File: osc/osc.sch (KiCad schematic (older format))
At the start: 21 parts, among them P1 CONN_1, P2 CONN_1, P3 CONN_1, P4 CONN_1, P5 CONN_1, P6 CONN_5X2, Y1 ASOF3S3, Y2 AOCJYR, Y3 AST3TQ-28, Y4 ASV

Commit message: Add footprint information for passive components.
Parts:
- C1: footprint (none) -> Capacitors_SMD:C_0603
- C2: footprint (none) -> Capacitors_SMD:C_1206
- JP1: footprint (none) -> Pin_Headers:Pin_Header_Straight_1x02
- P1, P2, P3, P4, P5: footprint (none) -> footprints:1pin
- P6: footprint (none) -> Pin_Headers:Pin_Header_Straight_2x05
- R1, R2, R3, R4, R5: footprint (none) -> Resistors_SMD:R_2512_HandSoldering
- R6, R7, R8: footprint (none) -> Resistors_SMD:R_0603_HandSoldering
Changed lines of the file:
@@
 F 0 "P5" H 2830 2350 40  0000 L CNN
 F 1 "CONN_1" H 2750 2405 30  0001 C CNN
-F 2 "" H 2750 2350 60  0000 C CNN
+F 2 "footprints:1pin" H 2750 2350 60  0001 C CNN
 F 3 "" H 2750 2350 60  0000 C CNN
 	1    2750 2350
@@
 F 0 "P2" H 2830 5250 40  0000 L CNN
 F 1 "CONN_1" H 2750 5305 30  0001 C CNN
-F 2 "" H 2750 5250 60  0000 C CNN
+F 2 "footprints:1pin" H 2750 5250 60  0001 C CNN
 F 3 "" H 2750 5250 60  0000 C CNN
 	1    2750 5250
@@
 F 0 "P1" H 9480 2350 40  0000 L CNN
 F 1 "CONN_1" H 9400 2405 30  0001 C CNN
-F 2 "" H 9400 2350 60  0000 C CNN
+F 2 "footprints:1pin" H 9400 2350 60  0001 C CNN
 F 3 "" H 9400 2350 60  0000 C CNN
 F 4 "Mill-Max" H 9400 2350 60  0001 C CNN "Vendor"
@@
 F 0 "P3" H 5480 4350 40  0000 L CNN
 F 1 "CONN_1" H 5400 4405 30  0001 C CNN
-F 2 "" H 5400 4350 60  0000 C CNN
+F 2 "footprints:1pin" H 5400 4350 60  0001 C CNN
 F 3 "" H 5400 4350 60  0000 C CNN
 	1    5400 4350
@@
 F 0 "P6" H 3750 3100 60  0000 C CNN
 F 1 "CONN_5X2" V 3750 2800 50  0000 C CNN
-F 2 "" H 3750 2800 60  0000 C CNN
+F 2 "Pin_Headers:Pin_Header_Straight_2x05" H 3750 2800 60  0001 C CNN
 F 3 "" H 3750 2800 60  0000 C CNN
 	1    3750 2800
@@
 F 0 "R1" V 3630 3600 40  0000 C CNN
 F 1 "10" V 3557 3601 40  0000 C CNN
-F 2 "" V 3480 3600 30  0000 C CNN
+F 2 "Resistors_SMD:R_2512_HandSoldering" V 3480 3600 30  0001 C CNN
 F 3 "" H 3550 3600 30  0000 C CNN
 	1    3550 3600
@@
 F 0 "R2" V 3730 3950 40  0000 C CNN
 F 1 "10" V 3657 3951 40  0000 C CNN
-F 2 "" V 3580 3950 30  0000 C CNN
+F 2 "Resistors_SMD:R_2512_HandSoldering" V 3580 3950 30  0001 C CNN
 F 3 "" H 3650 3950 30  0000 C CNN
 	1    3650 3950
@@
 F 0 "R3" V 3830 3600 40  0000 C CNN
 F 1 "10" V 3757 3601 40  0000 C CNN
-F 2 "" V 3680 3600 30  0000 C CNN
+F 2 "Resistors_SMD:R_2512_HandSoldering" V 3680 3600 30  0001 C CNN
 F 3 "" H 3750 3600 30  0000 C CNN
 	1    3750 3600
@@
 F 0 "R4" V 3930 3950 40  0000 C CNN
 F 1 "10" V 3857 3951 40  0000 C CNN
-F 2 "" V 3780 3950 30  0000 C CNN
+F 2 "Resistors_SMD:R_2512_HandSoldering" V 3780 3950 30  0001 C CNN
 F 3 "" H 3850 3950 30  0000 C CNN
 	1    3850 3950
@@
 F 0 "R5" V 4030 3600 40  0000 C CNN
 F 1 "10" V 3957 3601 40  0000 C CNN
-F 2 "" V 3880 3600 30  0000 C CNN
+F 2 "Resistors_SMD:R_2512_HandSoldering" V 3880 3600 30  0001 C CNN
 F 3 "" H 3950 3600 30  0000 C CNN
 	1    3950 3600
@@
 F 0 "C1" H 4850 2750 40  0000 L CNN
 F 1 "0.1uF" H 4856 2565 40  0000 L CNN
-F 2 "" H 4888 2500 30  0000 C CNN
+F 2 "Capacitors_SMD:C_0603" H 4888 2500 30  0001 C CNN
 F 3 "" H 4850 2650 60  0000 C CNN
 	1    4850 2650
@@
 F 0 "JP1" H 4450 2500 60  0000 C CNN
 F 1 "JUMPER" H 4450 2270 40  0000 C CNN
-F 2 "" H 4450 2350 60  0000 C CNN
+F 2 "Pin_Headers:Pin_Header_Straight_1x02" H 4450 2350 60  0001 C CNN
 F 3 "" H 4450 2350 60  0000 C CNN
 	1    4450 2350
@@
 F 0 "Y1" H 7350 3000 60  0000 C CNN
 F 1 "ASOF3S3" H 7300 2600 60  0000 L CNN
-F 2 "" H 7300 2950 60  0000 C CNN
+F 2 "" H 7300 2950 60  0001 C CNN
 F 3 "" H 7300 2950 60  0000 C CNN
 	1    7550 2800
@@
 F 0 "Y3" H 7350 4550 60  0000 C CNN
 F 1 "AST3TQ-28" H 7300 4150 60  0000 L CNN
-F 2 "" H 7300 4500 60  0000 C CNN
+F 2 "" H 7300 4500 60  0001 C CNN
 F 3 "" H 7300 4500 60  0000 C CNN
 	1    7550 4350
@@
 F 0 "Y4" H 7350 5350 60  0000 C CNN
 F 1 "ASV" H 7300 4950 60  0000 L CNN
-F 2 "" H 7300 5300 60  0000 C CNN
+F 2 "" H 7300 5300 60  0001 C CNN
 F 3 "" H 7300 5300 60  0000 C CNN
 	1    7550 5150
@@
 F 0 "Y2" H 7350 3800 60  0000 C CNN
 F 1 "AOCJYR" H 7300 3400 60  0000 L CNN
-F 2 "" H 7300 3750 60  0000 C CNN
+F 2 "" H 7300 3750 60  0001 C CNN
 F 3 "" H 7300 3750 60  0000 C CNN
 	1    7550 3600
@@
 F 0 "C2" H 5100 2750 40  0000 L CNN
 F 1 "10uF" H 5106 2565 40  0000 L CNN
-F 2 "" H 5138 2500 30  0000 C CNN
+F 2 "Capacitors_SMD:C_1206" H 5138 2500 30  0001 C CNN
 F 3 "" H 5100 2650 60  0000 C CNN
 	1    5100 2650
@@
 F 0 "R7" V 6430 3800 40  0000 C CNN
 F 1 "10k" V 6357 3801 40  0000 C CNN
-F 2 "" V 6280 3800 30  0000 C CNN
+F 2 "Resistors_SMD:R_0603_HandSoldering" V 6280 3800 30  0001 C CNN
 F 3 "" H 6350 3800 30  0000 C CNN
 	1    6350 3800
@@
 F 0 "P4" H 6130 7450 40  0000 L CNN
 F 1 "CONN_1" H 6050 7505 30  0001 C CNN
-F 2 "" H 6050 7450 60  0000 C CNN
+F 2 "footprints:1pin" H 6050 7450 60  0001 C CNN
 F 3 "" H 6050 7450 60  0000 C CNN
 F 4 "Mill-Max" H 6050 7450 60  0001 C CNN "Vendor"
@@
 F 0 "R6" V 5730 4700 40  0000 C CNN
 F 1 "10k" V 5657 4701 40  0000 C CNN
-F 2 "" V 5580 4700 30  0000 C CNN
+F 2 "Resistors_SMD:R_0603_HandSoldering" V 5580 4700 30  0001 C CNN
 F 3 "" H 5650 4700 30  0000 C CNN
 	1    5650 4700
@@
 F 0 "R8" V 6080 4350 40  0000 C CNN
 F 1 "0" V 6007 4351 40  0000 C CNN
-F 2 "" V 5930 4350 30  0000 C CNN
+F 2 "Resistors_SMD:R_0603_HandSoldering" V 5930 4350 30  0001 C CNN
 F 3 "" H 6000 4350 30  0000 C CNN
 	1    6000 4350

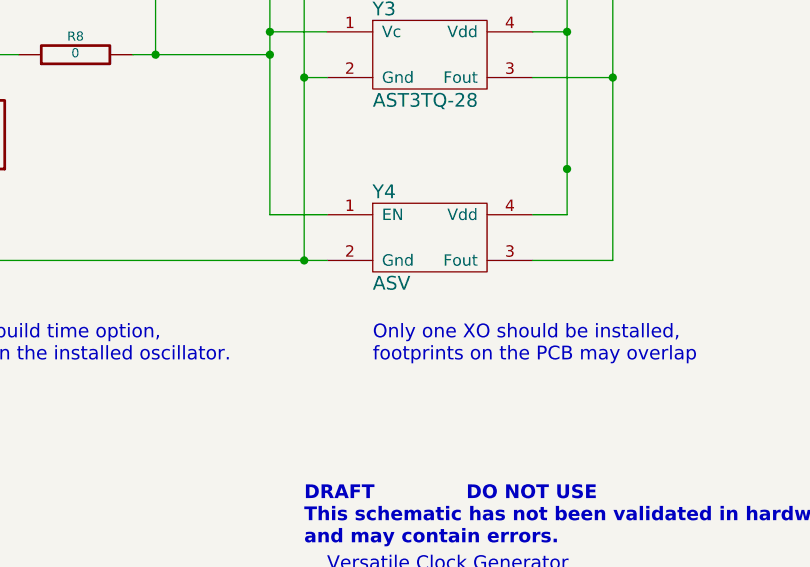
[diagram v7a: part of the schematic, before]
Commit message: Replace Y4 to M100: Con-Win LVCMOS in 2.5x3.2 mm package.
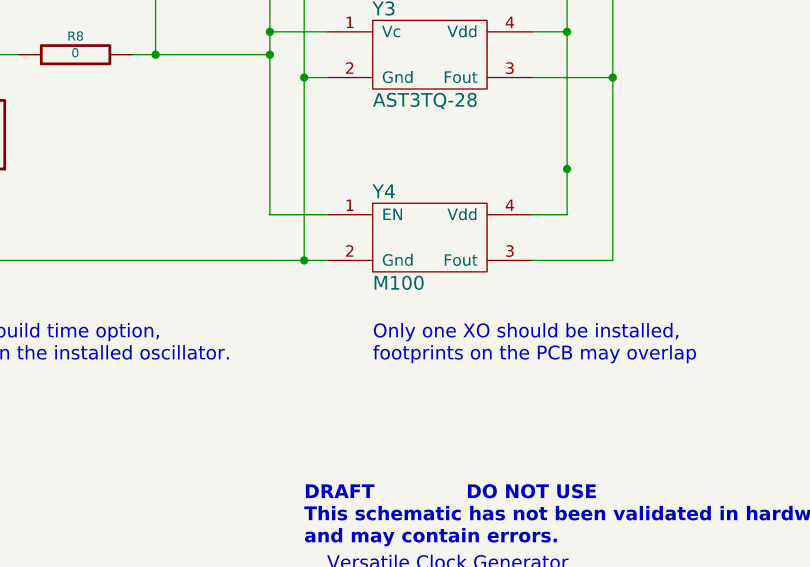
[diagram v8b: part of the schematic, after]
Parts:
- removed Y4: ASV, symbol ASV
- added Y4: M100, symbol M100
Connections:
- net Fout: now also Y4.3 (Fout)
- net GND: now also Y4.2 (Gnd)
- net Vc: now also Y4.1 (EN)
- net Vdd: now also Y4.4 (Vdd)
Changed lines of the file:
@@
-$EndComp
-$Comp
-L ASV Y4
-U 1 1 55F811B9
-P 7550 5150
-F 0 "Y4" H 7350 5350 60  0000 C CNN
-F 1 "ASV" H 7300 4950 60  0000 L CNN
-F 2 "" H 7300 5300 60  0001 C CNN
-F 3 "" H 7300 5300 60  0000 C CNN
-	1    7550 5150
-	1    0    0    -1
 $EndComp
 $Comp
@@
 Text Notes 5150 5700 0    60   ~ 0
 R6/R7/R8 -- build time option,\ndepending on the installed oscillator.
+$Comp
+L M100 Y4
+U 1 1 5700CE49
+P 7550 5150
+F 0 "Y4" H 7350 5350 60  0000 C CNN
+F 1 "M100" H 7300 4950 60  0000 L CNN
+F 2 "" H 7300 5300 60  0000 C CNN
+F 3 "" H 7300 5300 60  0000 C CNN
+	1    7550 5150
+	1    0    0    -1
+$EndComp
 $EndSCHEMATC
